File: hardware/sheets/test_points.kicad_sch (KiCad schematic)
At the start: 0 parts

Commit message: hw: draw LED matrix, row and column drivers and scan-stall safety (#8)
* repo: ignore KiCad local history

KiCad 10 keeps automatic snapshots in a .history folder (with its own
Git repository) next to the project. Ignore it, and make the hygiene
check reject it, so local history cannot be committed.

* hw: save schematic sheets in KiCad's own format

Opening and saving the project in KiCad 10 rewrites the generated
sheets and project file in its native layout. KiCad also merges seven
overlapping wire segments on the USB sheet. Nets, values and
footprints are unchanged, so committing this once keeps later edits
made in KiCad free of formatting churn.

* hw: add column driver and monostable symbols

Add a TLC59283 symbol with the RGE (VQFN-24) pin numbers from TI's pin
table; it uses KiCad's footprint for TI's RGE0024C package. Add a
single-unit SN74LVC1G123 symbol, because KiCad's version keeps the
supply pins in a separate unit.

* hw: draw matrix driver and LED matrix sheets

Columns: two cascaded TLC59283 sinks on 3V3. R_IREF is 2.94k, an
18.0 mA nominal setting (about 19.4 mA worst case with driver and
resistor tolerance), with a fitted 0 ohm in series, so adjustment can
only lower the current.

Rows: the TLC chain output, clock, latch and SAFE cross into the LED
rail through an SN74LVC8T245 translator. Four SN74HC595 on VLED drive
32 AO3401A high-side switches with 10k gate pull-ups, with row
pull-downs as unfitted options.

Scan-stall safety: every latch retriggers an SN74LVC1G123. TI
specifies 1.0-1.1 ms at 10k / 0.1 uF; with the fitted parts'
tolerances the timeout is 0.76-1.41 ms. The part has only a Q
output, so an inverter makes SAFE = NOT Q. SAFE forces the column
BLANK through an OR gate and tri-states the row registers, and the
MCU reads it. The matrix stays dark while the MCU is off or in
reset.

LED matrix: 1024 LEDs, anodes on the rows and cathodes on the
columns, drawn as row and column buses, on the front side with the
buttons (ADR 0008).

The pend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
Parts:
- added H1301, H1302, H1303, H1304: M2, MountingHole:MountingHole_2.2mm_M2, symbol Mechanical:MountingHole
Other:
- note added: "Test points and mechanical (Rev A) - index Test pads sit on the sheet of the circuit they probe (REQ-T2): - Power tree: SYS, VBAT, 3V3_REG, +3V3, VLED_REG, VLED, GND, EN_3V3, PG_3V3, LED_EN, VBAT_SENSE, VLED_SENSE, VBAT_MEAS_EN, SW_ON, PWR_SW_N - USB/charger/battery: VBUS, PMID, SYS, VBAT, TS, CHG_PG_N, QON, CHG_STAT, CC1, CC2, GND, I2C1 SDA/SCL - Debug: nRESET, SWDIO, SWDCLK, UART TX/RX, GND, si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"

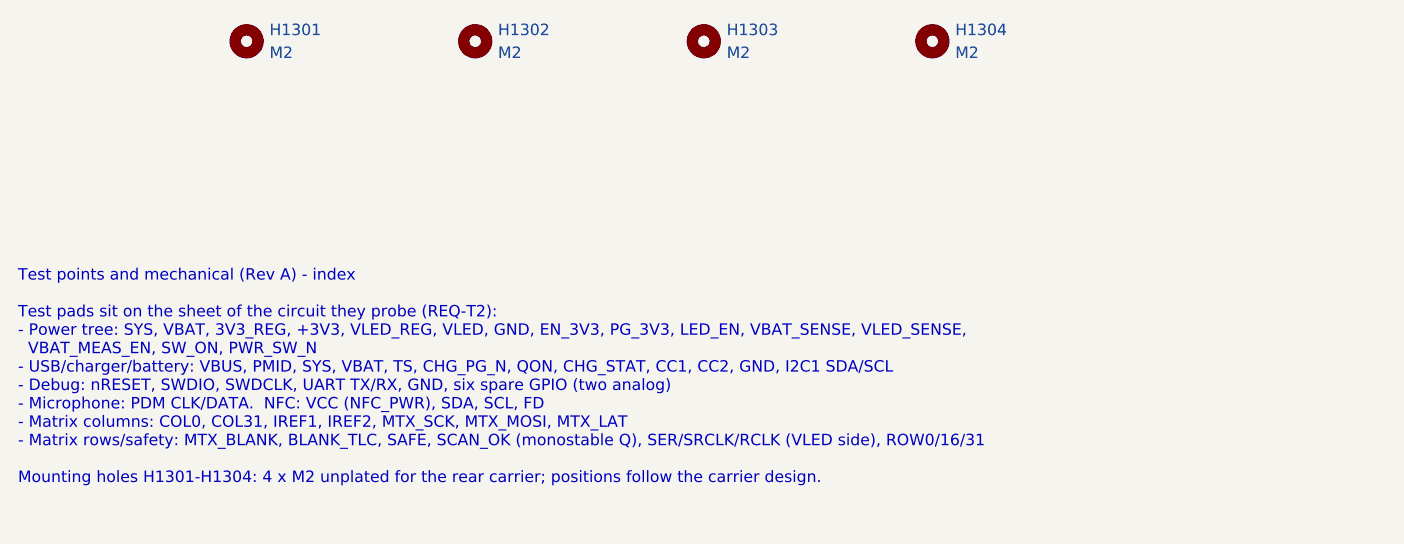
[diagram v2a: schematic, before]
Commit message: hw: apply layout footprint and test-point changes to the schematic
The matrix LEDs use the KENTO-pattern footprint, L1101 the PCB coil,
MK1001 the 0.6 mm hole footprint and J301 the project HRO copy.

Removes test points that duplicate others: TP303 and TP304, TP208 and
TP506, and TP501-TP503, whose signals are on the SWD header. Also
removes H1304, which the carrier does not use. Rail and GND test points
move to 0.8 mm pads.

nRESET now connects only the header's open-collector pin and the module
input. ERC reports that as not driven, so the error is excluded: the
nRF5340 has an internal pull-up on reset.
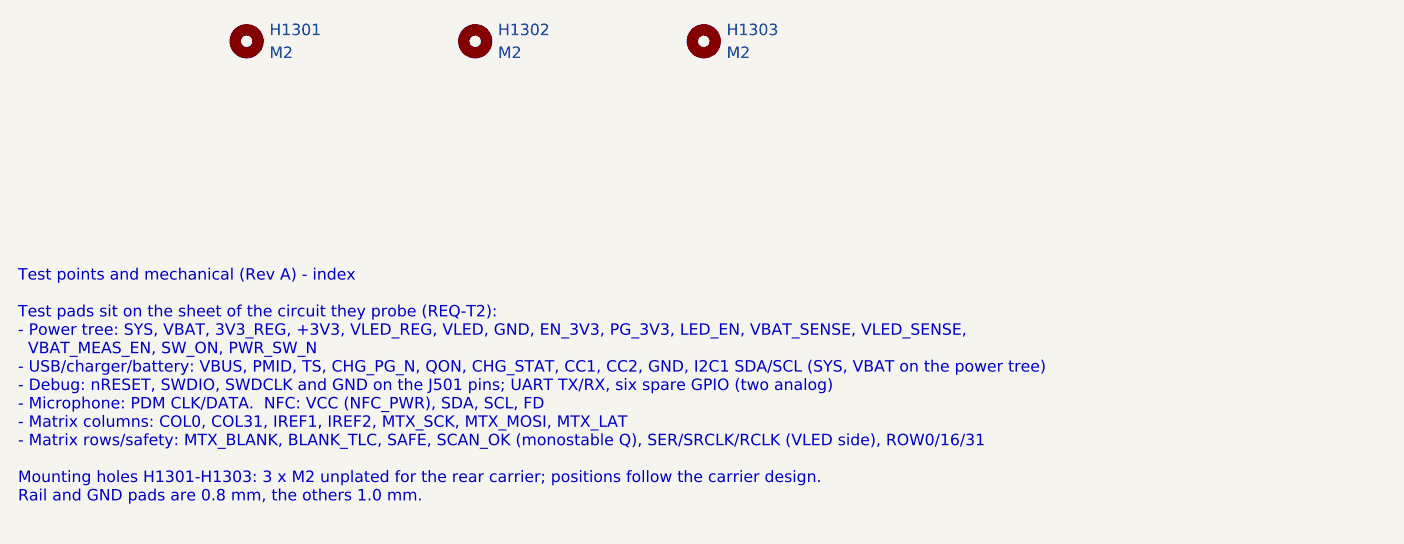
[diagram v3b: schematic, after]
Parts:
- removed H1304: M2, MountingHole:MountingHole_2.2mm_M2, symbol Mechanical:MountingHole
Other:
- note added: "Test points and mechanical (Rev A) - index Test pads sit on the sheet of the circuit they probe (REQ-T2): - Power tree: SYS, VBAT, 3V3_REG, +3V3, VLED_REG, VLED, GND, EN_3V3, PG_3V3, LED_EN, VBAT_SENSE, VLED_SENSE, VBAT_MEAS_EN, SW_ON, PWR_SW_N - USB/charger/battery: VBUS, PMID, TS, CHG_PG_N, QON, CHG_STAT, CC1, CC2, GND, I2C1 SDA/SCL (SYS, VBAT on the power tree) - Debug: nRESET, SWDIO, SWDCLK a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"
- note removed: "Test points and mechanical (Rev A) - index Test pads sit on the sheet of the circuit they probe (REQ-T2): - Power tree: SYS, VBAT, 3V3_REG, +3V3, VLED_REG, VLED, GND, EN_3V3, PG_3V3, LED_EN, VBAT_SENSE, VLED_SENSE, VBAT_MEAS_EN, SW_ON, PWR_SW_N - USB/charger/battery: VBUS, PMID, SYS, VBAT, TS, CHG_PG_N, QON, CHG_STAT, CC1, CC2, GND, I2C1 SDA/SCL - Debug: nRESET, SWDIO, SWDCLK, UART TX/RX, GND, si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"
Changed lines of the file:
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@@
 		(comment 2 "Schematic frozen for layout after review 2026-10-07; not for fabrication until the release gate")
 	)
-	(text "Test points and mechanical (Rev A) - index\n\nTest pads sit on the sheet of the circuit they probe (REQ-T2):\n- Power tree: SYS, VBAT, 3V3_REG, +3V3, VLED_REG, VLED, GND, EN_3V3, PG_3V3, LED_EN, VBAT_SENSE, VLED_SENSE,\n  VBAT_MEAS_EN, SW_ON, PWR_SW_N\n- USB/charger/battery: VBUS, PMID, SYS, VBAT, TS, CHG_PG_N, QON, CHG_STAT, CC1, CC2, GND, I2C1 SDA/SCL\n- Debug: nRESET, SWDIO, SWDCLK, UART TX/RX, GND, six spare GPIO (two analog)\n- Microphone: PDM CLK/DATA.  NFC: VCC (NFC_PWR), SDA, SCL, FD\n- Matrix columns: COL0, COL31, IREF1, IREF2, MTX_SCK, MTX_MOSI, MTX_LAT\n- Matrix rows/safety: MTX_BLANK, BLANK_TLC, SAFE, SCAN_OK (monostable Q), SER/SRCLK/RCLK (VLED side), ROW0/16/31\n\nMounting holes H1301-H1304: 4 x M2 unplated for the rear carrier; positions follow the carrier design."
+	(text "Test points and mechanical (Rev A) - index\n\nTest pads sit on the sheet of the circuit they probe (REQ-T2):\n- Power tree: SYS, VBAT, 3V3_REG, +3V3, VLED_REG, VLED, GND, EN_3V3, PG_3V3, LED_EN, VBAT_SENSE, VLED_SENSE,\n  VBAT_MEAS_EN, SW_ON, PWR_SW_N\n- USB/charger/battery: VBUS, PMID, TS, CHG_PG_N, QON, CHG_STAT, CC1, CC2, GND, I2C1 SDA/SCL (SYS, VBAT on the power tree)\n- Debug: nRESET, SWDIO, SWDCLK and GND on the J501 pins; UART TX/RX, six spare GPIO (two analog)\n- Microphone: PDM CLK/DATA.  NFC: VCC (NFC_PWR), SDA, SCL, FD\n- Matrix columns: COL0, COL31, IREF1, IREF2, MTX_SCK, MTX_MOSI, MTX_LAT\n- Matrix rows/safety: MTX_BLANK, BLANK_TLC, SAFE, SCAN_OK (monostable Q), SER/SRCLK/RCLK (VLED side), ROW0/16/31\n\nMounting holes H1301-H1303: 3 x M2 unplated for the rear carrier; positions follow the carrier design.\nRail and GND pads are 0.8 mm, the others 1.0 mm."
 		(exclude_from_sim no)
 		(at 50.8 88.9 0)
@@
 					(unit 1)
 				)
-			)
-		)
-	)
-	(symbol
-		(lib_id "Mechanical:MountingHole")
-		(at 152.4 63.5 0)
-		(unit 1)
-		(body_style 1)
-		(exclude_from_sim no)
-		(in_bom no)
-		(on_board yes)
-		(in_pos_files yes)
-		(dnp no)
-		(property "Reference" "H1304"
-			(at 154.94 62.23 0)
-			(show_name no)
-			(do_not_autoplace no)
-			(effects
-				(font
-					(size 1.27 1.27)
-				)
-				(justify left)
-			)
-		)
-		(property "Value" "M2"
-			(at 154.94 64.77 0)
-			(show_name no)
-			(do_not_autoplace no)
-			(effects
-				(font
-					(size 1.27 1.27)
-				)
-				(justify left)
-			)
-		)
-		(property "Footprint" "MountingHole:MountingHole_2.2mm_M2"
-			(at 152.4 63.5 0)
-			(hide yes)
-			(show_name no)
-			(do_not_autoplace no)
-			(effects
-				(font
-					(size 1.27 1.27)
-				)
-			)
-		)
-		(property "Datasheet" ""
-			(at 152.4 63.5 0)
-			(hide yes)
-			(show_name no)
-			(do_not_autoplace no)
-			(effects
-				(font
-					(size 1.27 1.27)
-				)
-			)
-		)
-		(property "Description" "Mounting Hole without connection"
-			(at 152.4 63.5 0)
-			(hide yes)
-			(show_name no)
-			(do_not_autoplace no)
-			(effects
-				(font
-					(size 1.27 1.27)
-				)
-			)
-		)
-		(property "Note" "Carrier mounting hole, unplated; position from the carrier design, outside the RF keep-out and NFC coil"
-			(at 152.4 63.5 0)
-			(hide yes)
-			(show_name no)
-			(do_not_autoplace no)
-			(effects
-				(font
-					(size 1.27 1.27)
-				)
-			)
-		)
-		(instances
-			(project "smart-led-badge"
-				(path "/fefc8d4a-8637-4143-b210-9149e35f9884/39857c90-bc81-42f1-ad6b-06d5802166c2"
-					(reference "H1304")
-					(unit 1)
-				)

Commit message: hw: switch U401 to the E73 nRF52840 module
The MDBT53-P1M cannot be sourced in time for the Rev A order, while
the E73-2G4M08S1C is stocked at JLCPCB (ADR 0015).

The E73 holds its DC/DC inductors and decoupling, so L401/L402 and
C403/C404 are removed. The nRF52840 has no internal 32.768 kHz load,
so C405/C406 are fitted with 12 pF; the value is calculated and still
needs checking against the Product Specification. All 29 module GPIO
are used: CHG_STAT is no longer read by the MCU, and the UART pads,
spare GPIO pads and IMU SPI-fallback links are removed. Pins Ebyte
marks as low-frequency carry only analog inputs or slow signals.
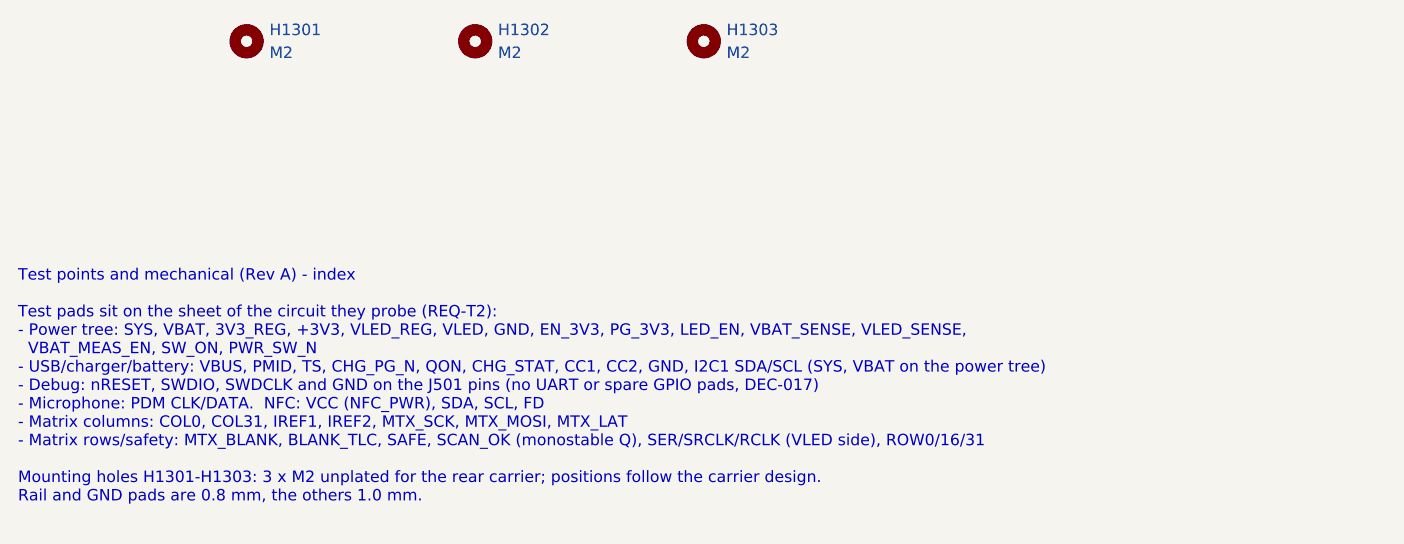
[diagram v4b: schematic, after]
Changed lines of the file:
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@@
 		(comment 2 "Schematic frozen for layout after review 2026-10-07; not for fabrication until the release gate")
 	)
-	(text "Test points and mechanical (Rev A) - index\n\nTest pads sit on the sheet of the circuit they probe (REQ-T2):\n- Power tree: SYS, VBAT, 3V3_REG, +3V3, VLED_REG, VLED, GND, EN_3V3, PG_3V3, LED_EN, VBAT_SENSE, VLED_SENSE,\n  VBAT_MEAS_EN, SW_ON, PWR_SW_N\n- USB/charger/battery: VBUS, PMID, TS, CHG_PG_N, QON, CHG_STAT, CC1, CC2, GND, I2C1 SDA/SCL (SYS, VBAT on the power tree)\n- Debug: nRESET, SWDIO, SWDCLK and GND on the J501 pins; UART TX/RX, six spare GPIO (two analog)\n- Microphone: PDM CLK/DATA.  NFC: VCC (NFC_PWR), SDA, SCL, FD\n- Matrix columns: COL0, COL31, IREF1, IREF2, MTX_SCK, MTX_MOSI, MTX_LAT\n- Matrix rows/safety: MTX_BLANK, BLANK_TLC, SAFE, SCAN_OK (monostable Q), SER/SRCLK/RCLK (VLED side), ROW0/16/31\n\nMounting holes H1301-H1303: 3 x M2 unplated for the rear carrier; positions follow the carrier design.\nRail and GND pads are 0.8 mm, the others 1.0 mm."
+	(text "Test points and mechanical (Rev A) - index\n\nTest pads sit on the sheet of the circuit they probe (REQ-T2):\n- Power tree: SYS, VBAT, 3V3_REG, +3V3, VLED_REG, VLED, GND, EN_3V3, PG_3V3, LED_EN, VBAT_SENSE, VLED_SENSE,\n  VBAT_MEAS_EN, SW_ON, PWR_SW_N\n- USB/charger/battery: VBUS, PMID, TS, CHG_PG_N, QON, CHG_STAT, CC1, CC2, GND, I2C1 SDA/SCL (SYS, VBAT on the power tree)\n- Debug: nRESET, SWDIO, SWDCLK and GND on the J501 pins (no UART or spare GPIO pads, DEC-017)\n- Microphone: PDM CLK/DATA.  NFC: VCC (NFC_PWR), SDA, SCL, FD\n- Matrix columns: COL0, COL31, IREF1, IREF2, MTX_SCK, MTX_MOSI, MTX_LAT\n- Matrix rows/safety: MTX_BLANK, BLANK_TLC, SAFE, SCAN_OK (monostable Q), SER/SRCLK/RCLK (VLED side), ROW0/16/31\n\nMounting holes H1301-H1303: 3 x M2 unplated for the rear carrier; positions follow the carrier design.\nRail and GND pads are 0.8 mm, the others 1.0 mm."
 		(exclude_from_sim no)
 		(at 50.8 88.9 0)

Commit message: hw: align notes with the routed Rev A board
The sheet notes and docs still described parts that were removed from
the routed board. Update them:
- NFC: no dedicated test pads fit; probe VCC, SCL, SDA and FD at the
  0402 pads of C1101, R1101, R1102 and R1103
- VLED: no trim positions; a different setting means replacing R210
  (about 30-36.5 kOhm for 4.4-5.2 V with R211 at 4.7 kOhm, calculated)
- charger TS: no RT2 position; TI's network needs a resistor added
  across the NTC
- the test-point index lists the pads that remain

Also refresh the hardware README board section (outline, silkscreen,
DRC warnings) and link ADR 0016. No electrical changes.
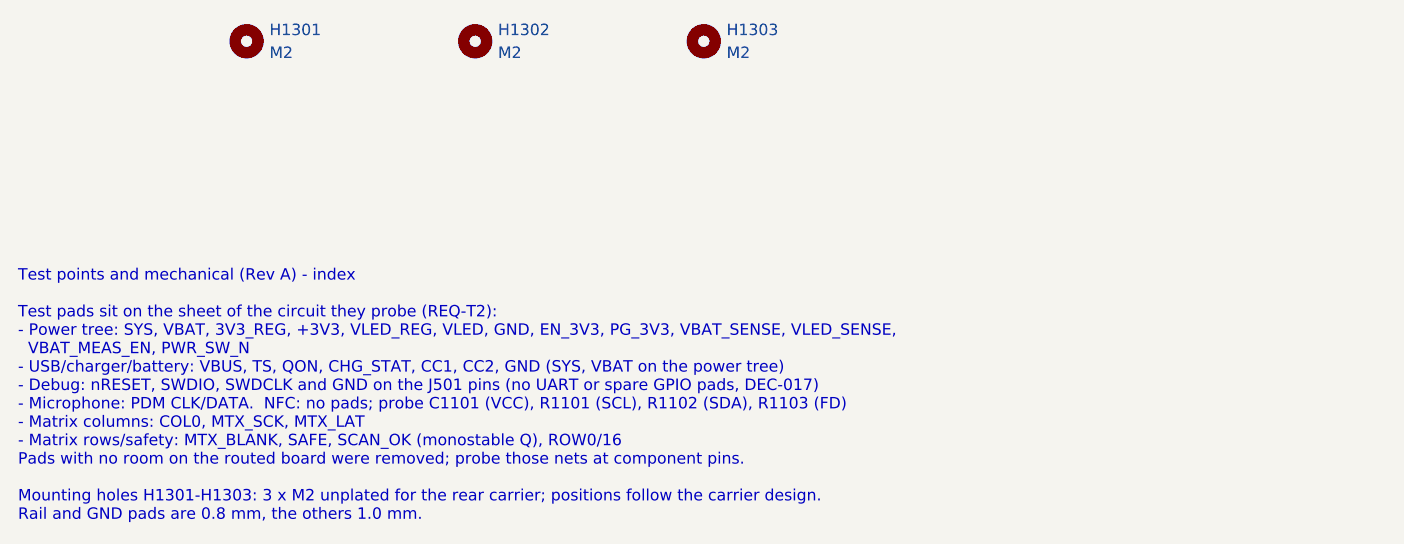
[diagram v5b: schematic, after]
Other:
- note added: "Test points and mechanical (Rev A) - index Test pads sit on the sheet of the circuit they probe (REQ-T2): - Power tree: SYS, VBAT, 3V3_REG, +3V3, VLED_REG, VLED, GND, EN_3V3, PG_3V3, VBAT_SENSE, VLED_SENSE, VBAT_MEAS_EN, PWR_SW_N - USB/charger/battery: VBUS, TS, QON, CHG_STAT, CC1, CC2, GND (SYS, VBAT on the power tree) - Debug: nRESET, SWDIO, SWDCLK and GND on the J501 pins (no UART or spare GPI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"
- note removed: "Test points and mechanical (Rev A) - index Test pads sit on the sheet of the circuit they probe (REQ-T2): - Power tree: SYS, VBAT, 3V3_REG, +3V3, VLED_REG, VLED, GND, EN_3V3, PG_3V3, LED_EN, VBAT_SENSE, VLED_SENSE, VBAT_MEAS_EN, SW_ON, PWR_SW_N - USB/charger/battery: VBUS, PMID, TS, CHG_PG_N, QON, CHG_STAT, CC1, CC2, GND, I2C1 SDA/SCL (SYS, VBAT on the power tree) - Debug: nRESET, SWDIO, SWDCLK a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"
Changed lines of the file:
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@@
 		(comment 2 "Schematic frozen for layout after review 2026-10-07; not for fabrication until the release gate")
 	)
-	(text "Test points and mechanical (Rev A) - index\n\nTest pads sit on the sheet of the circuit they probe (REQ-T2):\n- Power tree: SYS, VBAT, 3V3_REG, +3V3, VLED_REG, VLED, GND, EN_3V3, PG_3V3, LED_EN, VBAT_SENSE, VLED_SENSE,\n  VBAT_MEAS_EN, SW_ON, PWR_SW_N\n- USB/charger/battery: VBUS, PMID, TS, CHG_PG_N, QON, CHG_STAT, CC1, CC2, GND, I2C1 SDA/SCL (SYS, VBAT on the power tree)\n- Debug: nRESET, SWDIO, SWDCLK and GND on the J501 pins (no UART or spare GPIO pads, DEC-017)\n- Microphone: PDM CLK/DATA.  NFC: VCC (NFC_PWR), SDA, SCL, FD\n- Matrix columns: COL0, COL31, IREF1, IREF2, MTX_SCK, MTX_MOSI, MTX_LAT\n- Matrix rows/safety: MTX_BLANK, BLANK_TLC, SAFE, SCAN_OK (monostable Q), SER/SRCLK/RCLK (VLED side), ROW0/16/31\n\nMounting holes H1301-H1303: 3 x M2 unplated for the rear carrier; positions follow the carrier design.\nRail and GND pads are 0.8 mm, the others 1.0 mm."
+	(text "Test points and mechanical (Rev A) - index\n\nTest pads sit on the sheet of the circuit they probe (REQ-T2):\n- Power tree: SYS, VBAT, 3V3_REG, +3V3, VLED_REG, VLED, GND, EN_3V3, PG_3V3, VBAT_SENSE, VLED_SENSE,\n  VBAT_MEAS_EN, PWR_SW_N\n- USB/charger/battery: VBUS, TS, QON, CHG_STAT, CC1, CC2, GND (SYS, VBAT on the power tree)\n- Debug: nRESET, SWDIO, SWDCLK and GND on the J501 pins (no UART or spare GPIO pads, DEC-017)\n- Microphone: PDM CLK/DATA.  NFC: no pads; probe C1101 (VCC), R1101 (SCL), R1102 (SDA), R1103 (FD)\n- Matrix columns: COL0, MTX_SCK, MTX_LAT\n- Matrix rows/safety: MTX_BLANK, SAFE, SCAN_OK (monostable Q), ROW0/16\nPads with no room on the routed board were removed; probe those nets at component pins.\n\nMounting holes H1301-H1303: 3 x M2 unplated for the rear carrier; positions follow the carrier design.\nRail and GND pads are 0.8 mm, the others 1.0 mm."
 		(exclude_from_sim no)
 		(at 50.8 88.9 0)
